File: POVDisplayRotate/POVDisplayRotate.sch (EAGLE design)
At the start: 38 parts, among them U1 CY8CKIT-142, U2 STP08DP05, U3 STP08DP05, U4 STP08DP05, U5 MPQ4420Q

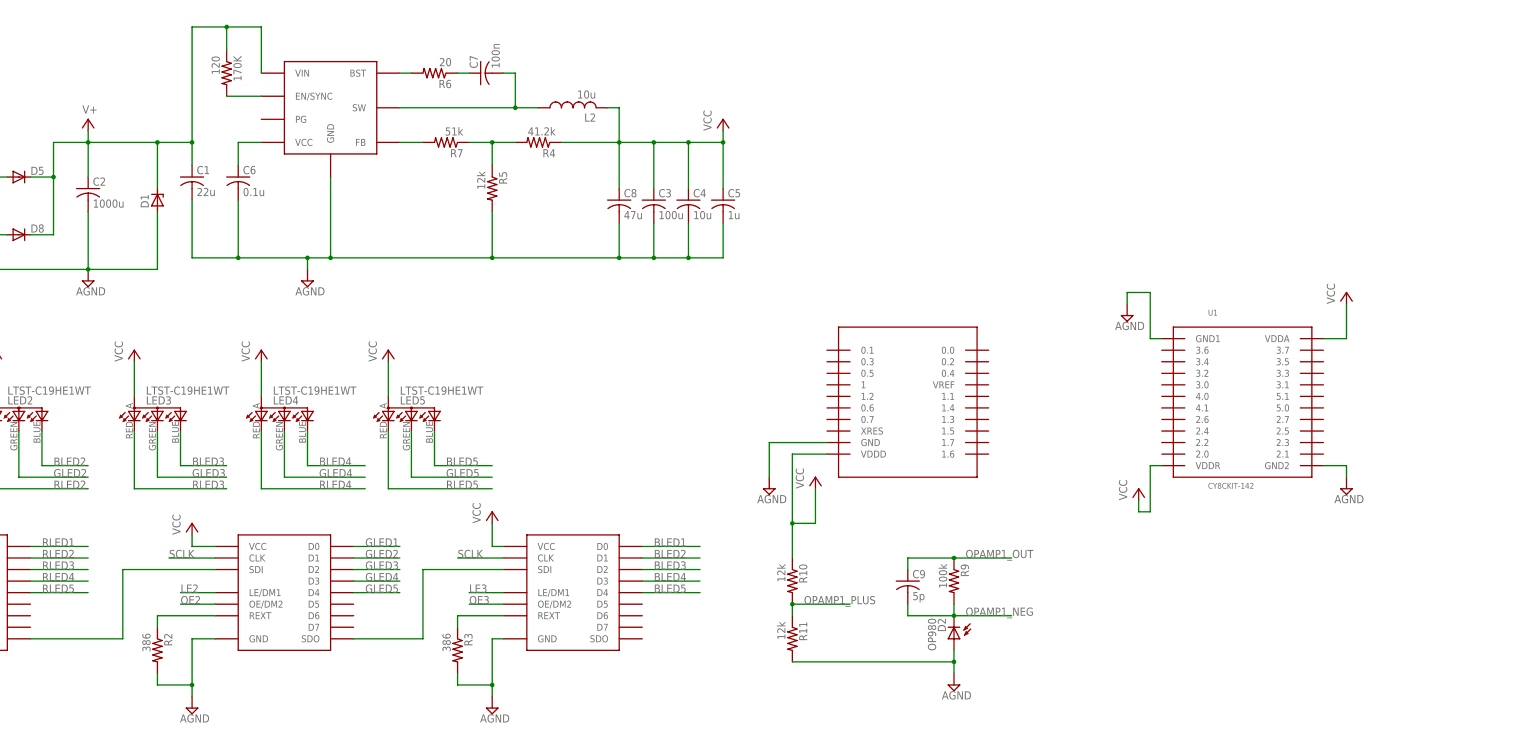
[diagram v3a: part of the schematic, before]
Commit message: Placed most of the components for the POVRotate. Working on PCB.
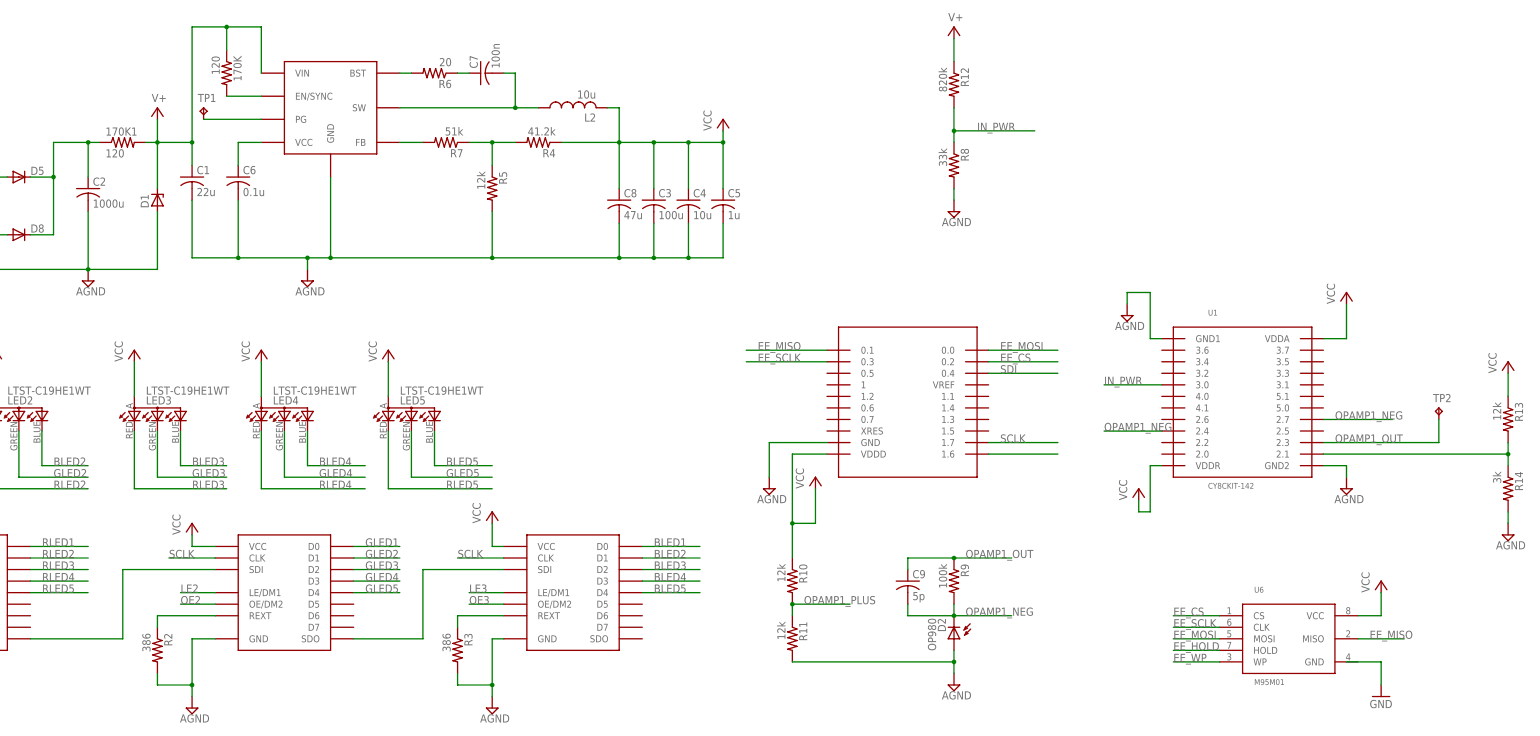
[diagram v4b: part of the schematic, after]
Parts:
- added 170K1: 120, resistor:R-US_R0603
- added R12: 820k, resistor:R-US_R0603
- added R13: 12k, resistor:R-US_R0603
- added R14: 3k, resistor:R-US_R0603
- added R8: 33k, resistor:R-US_R0603
- added TP1, TP2: TPB1,27, testpad:TPB1,27
- added U6: M95M01, NicksParts:M95M01
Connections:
- new net DAC_OUT: R13.2, R14.1, U1.2.1
- new net EE_CS: U1.0.2, U6.CS
- new net EE_HOLD: U6.HOLD
- new net EE_MISO: U1.0.1, U6.MISO
- new net EE_MOSI: U1.0.0, U6.MOSI
- new net EE_SCLK: U1.0.3, U6.CLK
- new net EE_WP: U6.WP
- new net IN_PWR: R12.2, R8.1, U1.3.0
- new net N$13: TP1.TP, U5.PG
- new net N$16: 170K1.1, C2.1, D5.C, D8.C
- new net N$3: U1.1.6
- net AGND: now also R14.2, R8.2
- net OPAMP1_NEG: now also U1.2.4, U1.2.7
- net OPAMP1_OUT: now also TP2.TP, U1.2.3
- net SCLK: now also U1.1.7
- net SDI: now also U1.0.4
- net V+: now also 170K1.2, R12.1; no longer C2.1, D5.C, D8.C
- net VCC: now also R13.1, U6.VCC

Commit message: Working on the routing of the POVRotate display.
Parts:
- removed 170K, 170K1: 120, resistor:R-US_R0603
- removed D7, D8: (no value), diode:DIODE-SOD123
- added C11: 0.1u, resistor:C-USC0603
- added D3, D4: (no value), diode:DIODE-SOD123
- added R15: 12k, resistor:R-US_R0603
- added R16: 3k, resistor:R-US_R0603
- C1: value 22u -> 100n; device resistor:C-USC0603 -> resistor:C-USC1210
- C10: value 100n -> 5p; device resistor:C-USC1210 -> resistor:C-USC0603
- C3: value 100u -> 22u; device resistor:C-USC1210 -> resistor:C-USC0603
- C4: value 10u -> 0.1u
- C5: value 1u -> 100n
- C6: value 0.1u -> 47u
- C7: value 100n -> 100u; device resistor:C-USC0603 -> resistor:C-USC1210
- C8: value 47u -> 10u
- C9: value 5p -> 1u
- D1: device diode:ZENER-DIODESMB -> diode:DIODE-SOD123; DIGIKEY MMSZ5232B-FDICT-ND -> B0540W-FDICT-ND
- D2: value OP980 -> (none); device NicksParts:OP980 -> diode:DIODE-SOD123; DIGIKEY 365-1908-1-ND -> B0540W-FDICT-ND
- D5: device diode:DIODE-SOD123 -> diode:ZENER-DIODESMB; DIGIKEY B0540W-FDICT-ND -> MMSZ5232B-FDICT-ND
- D6: value (none) -> OP980; device diode:DIODE-SOD123 -> NicksParts:OP980; DIGIKEY B0540W-FDICT-ND -> 365-1908-1-ND
- R13: value 12k -> 33k
- R14: value 3k -> 100k
- R2: value 386 -> 120
- R4: value 41.2k -> 120
- R5: value 12k -> 20
- R6: value 20 -> 51k
- R7: value 51k -> 386
- R8: value 33k -> 12k
- R9: value 100k -> 41.2k
- U1: value CY8CKIT-142 -> STP08DP05; device NicksParts:CY8CKIT-142 -> NicksParts:STP08DP05
- U3: value STP08DP05 -> MPQ4420Q; device NicksParts:STP08DP05 -> NicksParts:MPQ4420Q
- U5: value MPQ4420Q -> CY8CKIT-142; device NicksParts:MPQ4420Q -> NicksParts:CY8CKIT-142
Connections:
- removed net N$9: C7.2, L2.1, U5.SW
- new net SWOUT: C5.2, L2.1, U3.SW
- net AGND: now also C11.2, C7.2, C9.2, D5.A, R13.2, R16.2, R7.2, U5.GND1, U5.GND2; no longer C1.2, C5.2, D7.A, R14.2, R2.2, R5.2, U1.GND1, U1.GND2
- net DAC_OUT: now also R15.2, R16.1, U5.2.1; no longer R13.2, R14.1, U1.2.1
- net EE_CS: now also U5.0.2; no longer U1.0.2
- net EE_MISO: now also U5.0.1; no longer U1.0.1
- net EE_MOSI: now also U5.0.0; no longer U1.0.0
- net EE_SCLK: now also U5.0.3; no longer U1.0.3
- net GLED1: now also U2.D0; no longer U3.D0
- net GLED2: now also U2.D1; no longer U3.D1
- net GLED3: now also U2.D2; no longer U3.D2
- net GLED4: now also U2.D3; no longer U3.D3
- net GLED5: now also U2.D4; no longer U3.D4
- net IN_PWR: now also R13.1, U5.3.0; no longer R8.1, U1.3.0
- net LE1: now also U1.LE/DM1; no longer U2.LE/DM1
- net LE2: now also U2.LE/DM1; no longer U3.LE/DM1
- net N$1: now also C4.1, U3.VCC; no longer C6.1, U5.VCC
- net N$10: now also R3.1, U2.REXT; no longer R2.1, U3.REXT
- net N$11: now also U2.SDO; no longer U3.SDO
- net N$12: now also R7.1; no longer R3.1
- net N$13: now also U3.PG; no longer U5.PG
- net N$16: now also D3.C, D4.C, R2.1; no longer 170K1.1, D5.C, D8.C
- net N$18: now also U1.SDO, U2.SDI; no longer U2.SDO, U3.SDI
- net N$2: now also R4.2, U3.EN/SYNC; no longer 170K.2, U5.EN/SYNC
- net N$3: now also U5.1.6; no longer U1.1.6
- net N$4: now also R6.2, U3.FB; no longer R7.2, U5.FB
- net N$5: now also R6.1, R8.1, R9.2; no longer R4.2, R5.1, R7.1
- net N$6: now also U1.REXT; no longer U2.REXT
- net N$7: now also R5.2, U3.BST; no longer R6.2, U5.BST
- net N$8: now also C5.1, R5.1; no longer C7.1, R6.1
- net NEG_COIL: now also C1.2, D2.C, D4.A; no longer C10.2, D7.C, D8.A
- net OE1: now also U1.OE/DM2; no longer U2.OE/DM2
- net OE2: now also U2.OE/DM2; no longer U3.OE/DM2
- net OPAMP1_NEG: now also C10.2, D6.C, R14.2, U5.2.4, U5.2.7; no longer C9.2, D2.C, R9.2, U1.2.4, U1.2.7
- net OPAMP1_OUT: now also C10.1, R14.1, U5.2.3; no longer C9.1, R9.1, U1.2.3
- net POS_COIL: now also C1.1, D1.C, D3.A; no longer C10.1, D5.A, D6.C
- net RLED1: now also U1.D0; no longer U2.D0
- net RLED2: now also U1.D1; no longer U2.D1
- net RLED3: now also U1.D2; no longer U2.D2
- net RLED4: now also U1.D3; no longer U2.D3
- net RLED5: now also U1.D4; no longer U2.D4
- net SCLK: now also U1.CLK, U5.1.7; no longer U1.1.7, U3.CLK
- net SDI: now also U1.SDI, U5.0.4; no longer U1.0.4, U2.SDI
- net V+: now also C11.1, C3.1, D5.C, R2.2, R4.1, U3.VIN; no longer 170K.1, 170K1.2, C1.1, D1.C, U5.VIN
- net VCC: now also C6.1, C7.1, C9.1, R15.1, R9.1, U1.VCC, U5.VDDA, U5.VDDD, U5.VDDR; no longer C3.1, C4.1, C5.1, R13.1, R4.1, U1.VDDA, U1.VDDD, U1.VDDR, U3.VCC
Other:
- moved on the sheet: C1, C10, C2, C3, C4, C5, C6, C7, C8, C9, R13, R14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

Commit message: More routing.
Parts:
- removed R7: 386, resistor:R-US_R0603
- removed U4: STP08DP05, NicksParts:STP08DP05
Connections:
- removed net LE3: U4.LE/DM1
- removed net N$11: U2.SDO, U4.SDI
- removed net N$12: R7.1, U4.REXT
- removed net OE3: U4.OE/DM2
- net AGND: no longer R7.2, U4.GND
- net BLED1: now also U1.D2; no longer U4.D0
- net BLED2: now also U1.D5; no longer U4.D1
- net BLED3: now also U2.D0; no longer U4.D2
- net BLED4: now also U2.D3; no longer U4.D3
- net BLED5: now also U2.D6; no longer U4.D4
- net GLED1: now also U1.D1; no longer U2.D0
- net GLED2: now also U1.D4; no longer U2.D1
- net GLED3: now also U1.D7; no longer U2.D2
- net GLED4: now also U2.D2; no longer U2.D3
- net GLED5: now also U2.D5; no longer U2.D4
- net RLED2: now also U1.D3; no longer U1.D1
- net RLED3: now also U1.D6; no longer U1.D2
- net RLED4: now also U2.D1; no longer U1.D3
- net RLED5: now also U2.D4; no longer U1.D4
- net SCLK: no longer U4.CLK
- net VCC: no longer U4.VCC

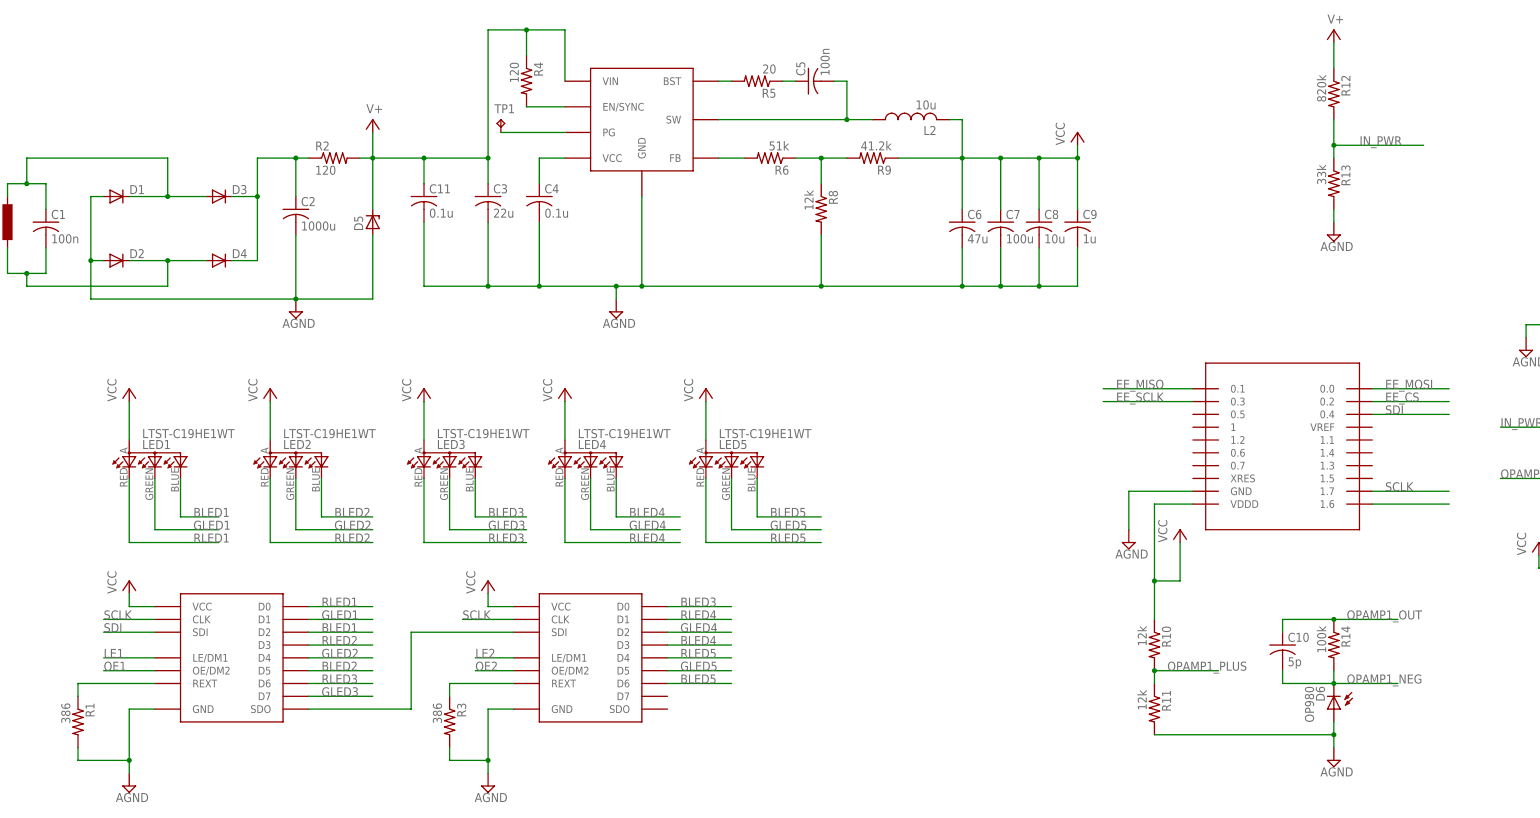
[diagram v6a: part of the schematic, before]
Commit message: Added additional datasheets and digikey part numbers.
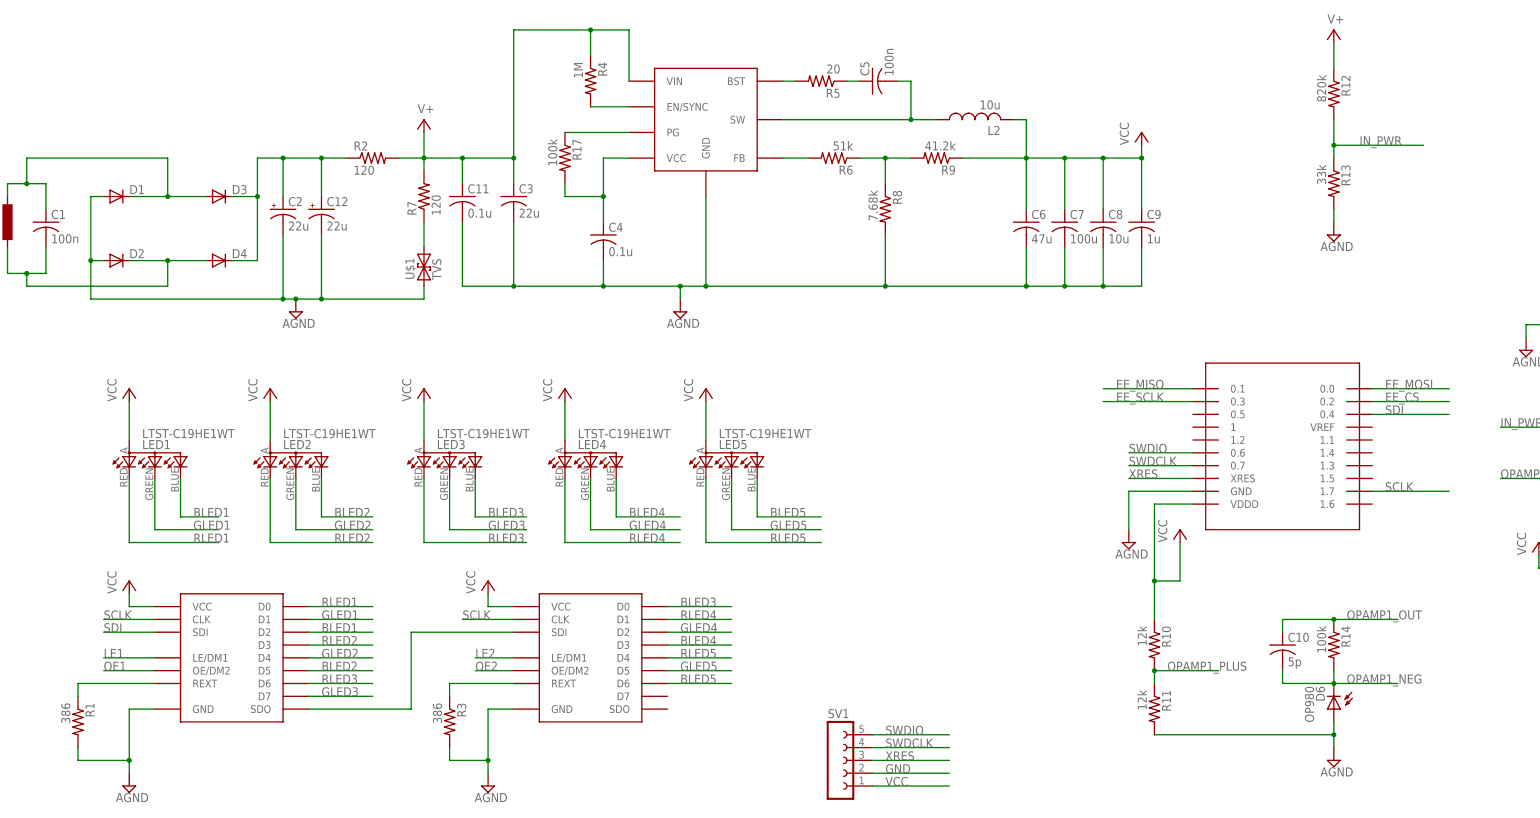
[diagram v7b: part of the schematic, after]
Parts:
- removed D5: (no value), diode:ZENER-DIODESMB
- removed TP1: TPB1,27, testpad:TPB1,27
- added C12: 22u, resistor:CPOL-USC
- added R17: 100k, resistor:R-US_R0603
- added R7: 120, resistor:R-US_R0603
- added SV1: (no value), con-lsta:FE05-1
- added U$1: TVS, NicksParts:TVS
- C11, C4: DIGIKEY (none) -> 490-6505-1-ND
- C2: value 1000u -> 22u; device resistor:C-USC1210 -> resistor:CPOL-USC; DIGIKEY (none) -> PCE5022CT-ND
- C3: device resistor:C-USC0603 -> resistor:C-USC0805; DIGIKEY (none) -> 445-14428-1-ND
- L2: DIGIKEY (none) -> 587-1625-1-ND
- R4: value 120 -> 1M
- R8: value 12k -> 7.68k
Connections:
- removed net N$16: C2.1, D3.C, D4.C, R2.1
- new net GND: SV1.2
- new net N$11: R7.1, U$1.2
- new net SWDCLK: SV1.4, U5.0.7
- new net SWDIO: SV1.5, U5.0.6
- new net XRES: SV1.3, U5.XRES
- net AGND: now also C12.-, C2.-, U$1.1; no longer C2.2, D5.A
- net N$1: now also R17.2
- net N$13: now also R17.1; no longer TP1.TP
- net N$3: now also C12.+, C2.+, D3.C, D4.C, R2.1; no longer U5.1.6
- net V+: now also R7.2; no longer D5.C
- net VCC: now also SV1.1
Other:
- moved on the sheet: C11, C3, C4, C5, C6, C7, C8, C9, L2, R2, R4, R5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

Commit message: Completed the routing of the POV Rotate board
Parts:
- removed U6: M95M01, NicksParts:M95M01
- added U4: CY8CKIT-142, NicksParts:CY8CKIT-142
- C10: value 5p -> 10u
- C11: value 0.1u -> 1u; DIGIKEY 490-6505-1-ND -> (none)
- C12: value 22u -> 5p; device resistor:CPOL-USC -> resistor:C-USC0603; DIGIKEY PCE5022CT-ND -> (none)
- C3: device resistor:C-USC0805 -> resistor:CPOL-USC; DIGIKEY 445-14428-1-ND -> PCE5022CT-ND
- C5: value 100n -> 22u; device resistor:C-USC0603 -> resistor:C-USC0805; DIGIKEY (none) -> 445-14428-1-ND
- C6: value 47u -> 0.1u; DIGIKEY (none) -> 490-6505-1-ND
- C7: value 100u -> 100n; device resistor:C-USC1210 -> resistor:C-USC0603
- C8: value 10u -> 47u
- C9: value 1u -> 100u; device resistor:C-USC0603 -> resistor:C-USC1210
- R10: value 12k -> 41.2k
- R12: value 820k -> 12k
- R13: value 33k -> 820k
- R14: value 100k -> 33k
- R15: value 12k -> 100k
- R16: value 3k -> 12k
- R17: value 100k -> 3k
- R3: value 386 -> 120
- R4: value 1M -> 386
- R5: value 20 -> 100k
- R6: value 51k -> 1M
- R7: value 120 -> 20
- R8: value 7.68k -> 51k
- R9: value 41.2k -> 7.68k
- U5: value CY8CKIT-142 -> M95M01; device NicksParts:CY8CKIT-142 -> NicksParts:M95M01; DIGIKEY (none) -> 497-14359-1-ND
- renumbered U$1 to D5
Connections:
- removed net AGND: C11.2, C12.-, C2.-, C3.2, C4.2, C6.2, C7.2, C8.2, C9.2, D1.A, D2.A, D5.1, D6.A, R1.2, R11.2, R13.2, R16.2, R3.2, R8.2, U1.GND, U2.GND, U3.GND, U5.GND, U5.GND1, U5.GND2
- new net N$17: C2.-, C3.-, D1.A, D2.A, D5.1
- net DAC_OUT: now also R16.2, R17.1, U4.2.1; no longer R15.2, R16.1, U5.2.1
- net EE_CS: now also U4.0.2, U5.CS; no longer U5.0.2, U6.CS
- net EE_HOLD: now also U5.HOLD; no longer U6.HOLD
- net EE_MISO: now also U4.0.1, U5.MISO; no longer U5.0.1, U6.MISO
- net EE_MOSI: now also U4.0.0, U5.MOSI; no longer U5.0.0, U6.MOSI
- net EE_SCLK: now also U4.0.3, U5.CLK; no longer U5.0.3, U6.CLK
- net EE_WP: now also U5.WP; no longer U6.WP
- net GND: now also C10.2, C11.2, C4.2, C5.2, C6.2, C8.2, C9.2, D6.A, R1.2, R12.2, R14.2, R17.2, R4.2, R9.2, U1.GND, U2.GND, U3.GND, U4.GND, U4.GND1, U4.GND2
- net IN_PWR: now also R13.2, R14.1, U4.3.0; no longer R12.2, R13.1, U5.3.0
- net N$1: now also C6.1, R5.2; no longer C4.1, R17.2
- net N$10: now also R4.1; no longer R3.1
- net N$11: now also R3.1; no longer R7.1
- net N$13: now also R5.1; no longer R17.1
- net N$2: now also R6.2; no longer R4.2
- net N$3: now also C3.+; no longer C12.+
- net N$4: now also R8.2; no longer R6.2
- net N$5: now also R10.2, R9.1; no longer R6.1, R9.2
- net N$7: now also R7.2; no longer R5.2
- net N$8: now also C7.1, R7.1; no longer C5.1, R5.1
- net OPAMP1_NEG: now also C12.2, R15.2, U4.2.4, U4.2.7; no longer C10.2, R14.2, U5.2.4, U5.2.7
- net OPAMP1_OUT: now also C12.1, R15.1, U4.2.3; no longer C10.1, R14.1, U5.2.3
- net OPAMP1_PLUS: now also R11.2, R12.1; no longer R10.2, R11.1
- net SCLK: now also U4.1.7; no longer U5.1.7
- net SDI: now also U4.0.4; no longer U5.0.4
- net SWDCLK: now also U4.0.7; no longer U5.0.7
- net SWDIO: now also U4.0.6; no longer U5.0.6
- net SWOUT: now also C7.2; no longer C5.2
- net V+: now also C4.1, C5.1, R13.1, R3.2, R6.1; no longer C11.1, C3.1, R12.1, R4.1, R7.2
- net VCC: now also C10.1, C11.1, R11.1, R16.1, U4.VDDA, U4.VDDD, U4.VDDR, U5.VCC; no longer C6.1, C7.1, R15.1, R9.1, U5.VDDA, U5.VDDD, U5.VDDR, U6.VCC
- net XRES: now also U4.XRES; no longer U5.XRES
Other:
- moved on the sheet: C10, C11, C4, C5, C6, C7, C8, C9, R10, R11, R12, R13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
